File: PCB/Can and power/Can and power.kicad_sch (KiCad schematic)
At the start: 31 parts, among them J1 TPS54232DR, J2 ESP32, J3 12V, J4 C_H, J5 C_L, J6 GND, U1 SN65HVD230

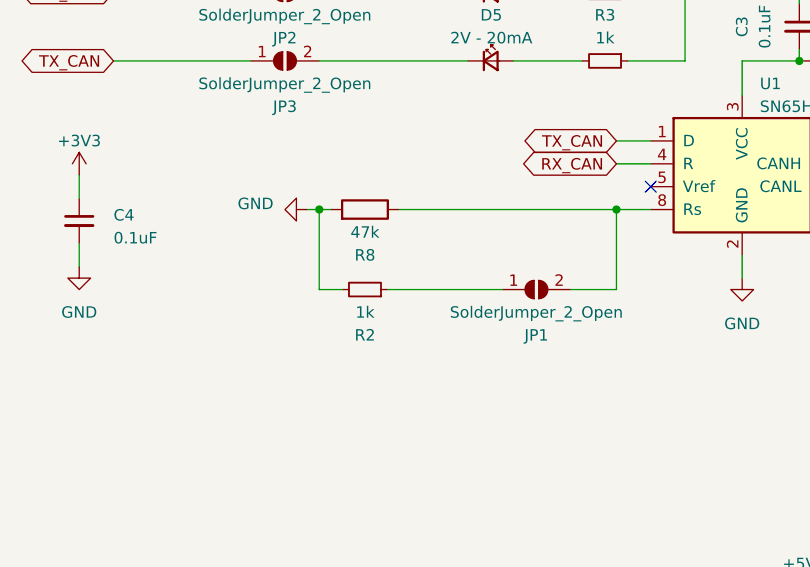
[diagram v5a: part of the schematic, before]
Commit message: Resistor correction
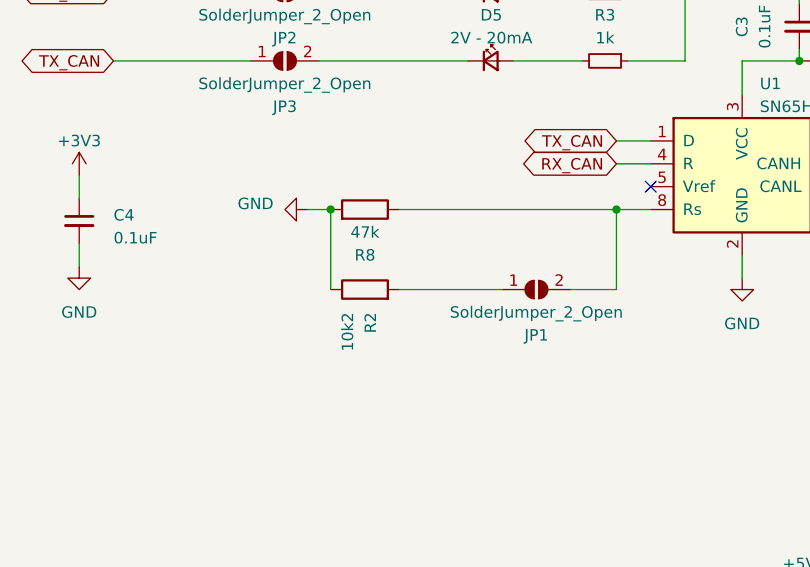
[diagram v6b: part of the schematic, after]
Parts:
- removed R2: 1k, Resistor_SMD:R_0603_1608Metric, symbol Device:R_Small
- added R2: 10k2, Resistor_SMD:R_0603_1608Metric, symbol Device:R
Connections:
- net GND: now also R2.1
- net at JP1.1 (A): now also R2.2
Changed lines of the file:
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@@
   (junction (at 153.67 143.51) (diameter 0) (color 0 0 0 0)
   )
-  (junction (at 144.78 72.39) (diameter 0) (color 0 0 0 0)
+  (junction (at 146.05 72.39) (diameter 0) (color 0 0 0 0)
   )
   (junction (at 198.12 119.38) (diameter 0) (color 0 0 0 0)
@@
     (stroke (width 0) (type default))
   )
+  (wire (pts (xy 153.67 81.28) (xy 165.1 81.28))
+    (stroke (width 0) (type default))
+  )
   (wire (pts (xy 60.96 163.83) (xy 66.04 163.83))
     (stroke (width 0) (type default))
@@
     (stroke (width 0) (type default))
   )
-  (wire (pts (xy 152.4 81.28) (xy 165.1 81.28))
-    (stroke (width 0) (type default))
-  )
   (wire (pts (xy 179.07 55.88) (xy 185.42 55.88))
     (stroke (width 0) (type default))
@@
     (stroke (width 0) (type default))
   )
-  (wire (pts (xy 144.78 72.39) (xy 143.51 72.39))
-    (stroke (width 0) (type default))
-  )
   (wire (pts (xy 121.92 48.26) (xy 137.16 48.26))
     (stroke (width 0) (type default))
   )
-  (wire (pts (xy 144.78 81.28) (xy 144.78 72.39))
-    (stroke (width 0) (type default))
-  )
   (wire (pts (xy 31.75 161.29) (xy 40.64 161.29))
     (stroke (width 0) (type default))
@@
     (stroke (width 0) (type default))
   )
+  (wire (pts (xy 143.51 72.39) (xy 146.05 72.39))
+    (stroke (width 0) (type default))
+  )
   (wire (pts (xy 207.01 119.38) (xy 207.01 120.65))
     (stroke (width 0) (type default))
@@
     (stroke (width 0) (type default))
   )
-  (wire (pts (xy 147.32 81.28) (xy 144.78 81.28))
-    (stroke (width 0) (type default))
-  )
   (wire (pts (xy 172.72 81.28) (xy 177.8 81.28))
     (stroke (width 0) (type default))
@@
     (stroke (width 0) (type default))
   )
-  (wire (pts (xy 146.05 72.39) (xy 144.78 72.39))
+  (wire (pts (xy 146.05 72.39) (xy 146.05 81.28))
     (stroke (width 0) (type default))
   )
@@
     )
   )
+  (symbol (lib_id "Device:R") (at 149.86 81.28 90) (unit 1)
+    (in_bom yes) (on_board yes) (dnp no)
+    (property "Reference" "R2" (at 150.495 83.82 0)
+      (effects (font (size 1.27 1.27)) (justify right))
+    )
+    (property "Value" "10k2" (at 147.955 83.82 0)
+      (effects (font (size 1.27 1.27)) (justify right))
+    )
+    (property "Footprint" "Resistor_SMD:R_0603_1608Metric" (at 149.86 83.058 90)
+      (effects (font (size 1.27 1.27)) hide)
+    )
+    (property "Datasheet" "https://www.yageo.com/upload/media/product/products/datasheet/rchip/PYu-RC_Group_51_RoHS_L_12.pdf" (at 149.86 81.28 0)
+      (effects (font (size 1.27 1.27)) hide)
+    )
+    (property "Description" "RES 10.2K OHM 1% 1/10W 0603" (at 149.86 81.28 0)
+      (effects (font (size 1.27 1.27)) hide)
+    )
+    (property "Manufacturer_Name" "YAGEO" (at 149.86 81.28 0)
+      (effects (font (size 1.27 1.27)) hide)
+    )
+    (property "Manufacturer_Part_Number" "RC0603FR-0710K2L" (at 149.86 81.28 0)
+      (effects (font (size 1.27 1.27)) hide)
+    )
+    (pin "1")
+    (pin "2")
+    (instances
+      (project "Can and power"
+        (path "/81a7cfcd-072f-485b-9296-819a4dd752de"
+          (reference "R2") (unit 1)
+        )
+      )
+    )
+  )
   (symbol (lib_id "Device:R") (at 149.86 72.39 270) (mirror x) (unit 1)
     (in_bom yes) (on_board yes) (dnp no)
@@
         )
       )
-    )
-  )
-  (symbol (lib_id "Device:R_Small") (at 149.86 81.28 270) (mirror x) (unit 1)
-    (in_bom yes) (on_board yes) (dnp no)
-    (property "Reference" "R2" (at 149.86 86.36 90)
-      (effects (font (size 1.27 1.27)))
-    )
-    (property "Value" "1k" (at 149.86 83.82 90)
-      (effects (font (size 1.27 1.27)))
-    )
-    (property "Footprint" "Resistor_SMD:R_0603_1608Metric" (at 149.86 81.28 0)
-      (effects (font (size 1.27 1.27)) hide)
-    )
-    (property "Datasheet" "https://www.yageo.com/upload/media/product/products/datasheet/rchip/PYu-RC_Group_51_RoHS_L_12.pdf" (at 149.86 81.28 0)
-      (effects (font (size 1.27 1.27)) hide)
-    )
-    (property "Description" "RES 1K OHM 1% 1/10W 0603" (at 149.86 81.28 0)
-      (effects (font (size 1.27 1.27)) hide)
-    )
-    (property "Manufacturer_Name" "YAGEO" (at 149.86 81.28 0)
-      (effects (font (size 1.27 1.27)) hide)
-    )
-    (property "Manufacturer_Part_Number" "RC0603FR-071KL" (at 149.86 81.28 0)
-      (effects (font (size 1.27 1.27)) hide)
-    )
-    (pin "1")
-    (pin "2")
-    (instances
-      (project "Can and power"
-        (path "/81a7cfcd-072f-485b-9296-819a4dd752de"
-          (reference "R2") (unit 1)
-        )
-      )

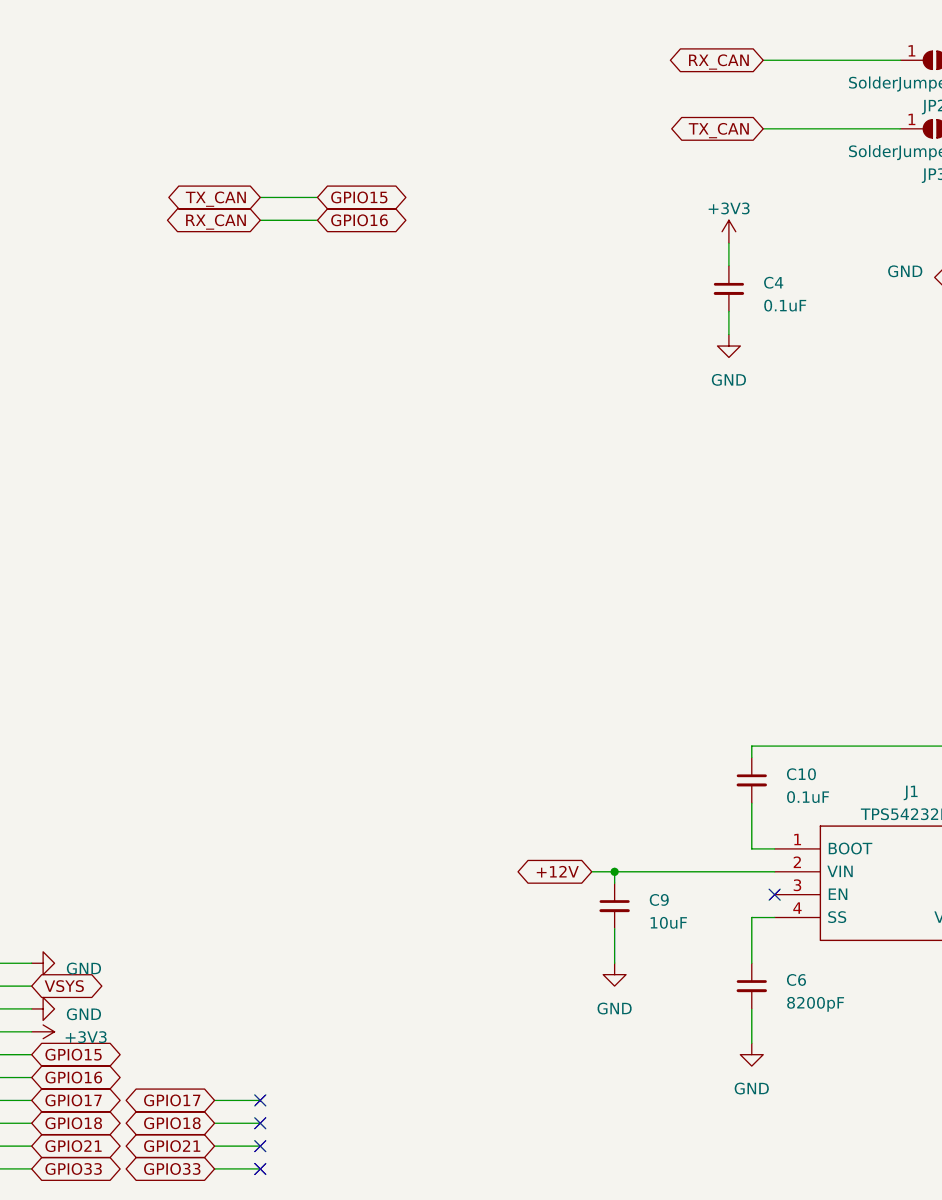
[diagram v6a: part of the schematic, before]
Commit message: New shield design
New shield design. MCP2515 is gone and transceiver has moved to SN65HVD230
Enable pin on the converter is used to cut off the uC when below 12V. Resistor values may have to change.
No real protection on start up stage -> might need another layer for that
Updated INO to reflect the changes in pinout
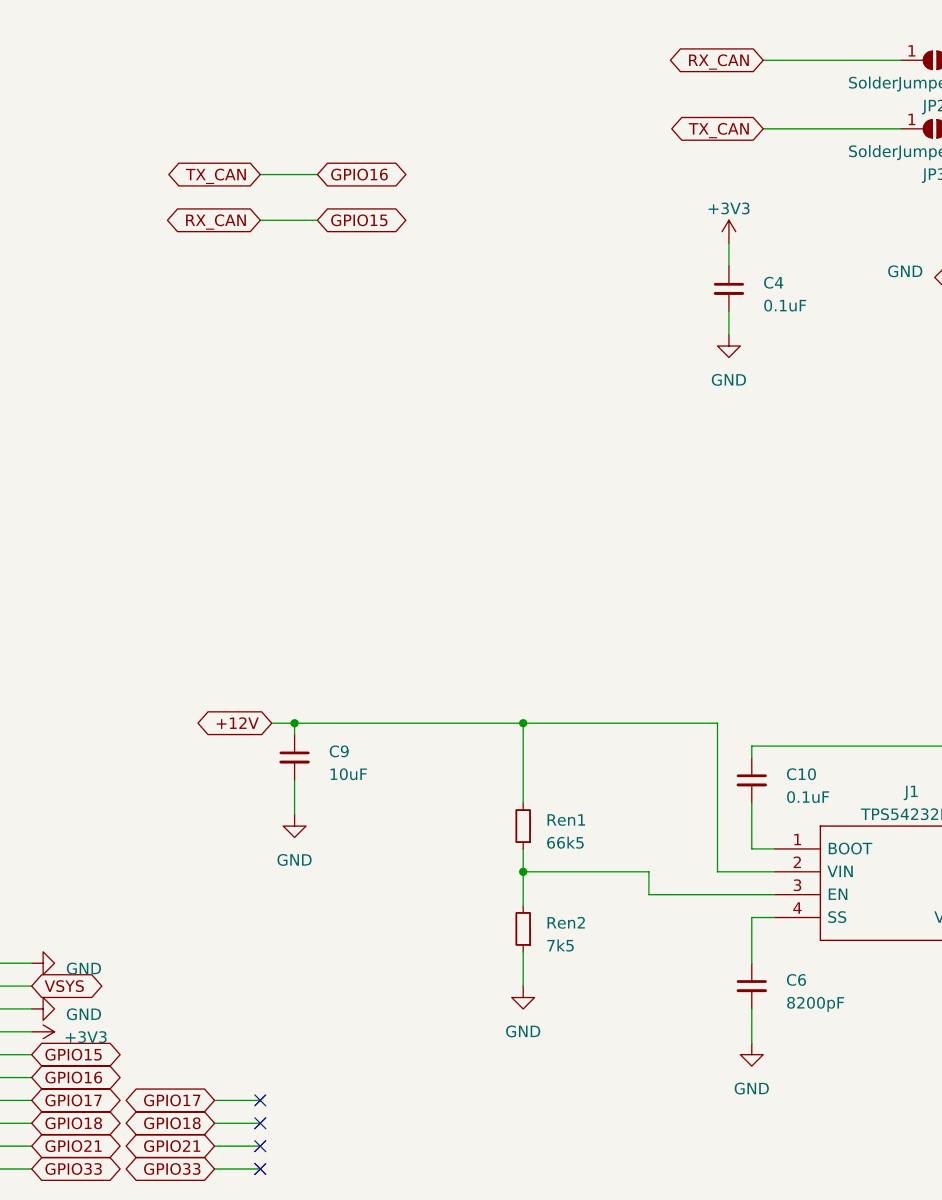
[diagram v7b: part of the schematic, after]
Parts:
- added Ren1: 66k5, Resistor_SMD:R_0603_1608Metric, symbol Device:R_Small
- added Ren2: 7k5, Resistor_SMD:R_0603_1608Metric, symbol Device:R_Small
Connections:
- net +12V: now also Ren1.2
- net GND: now also Ren2.1
- net GPIO15: now also JP2.1 (A), U1.4 (R); no longer JP3.1 (A), U1.1 (D)
- net GPIO16: now also JP3.1 (A), U1.1 (D); no longer JP2.1 (A), U1.4 (R)
- net at J1.3 (EN): now also Ren1.1, Ren2.2
- no-connect marks 6 -> 5
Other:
- moved on the sheet: C9

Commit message: CAD reference update
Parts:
- U1: Manufacturer_Name (none) -> Texas Instruments; Manufacturer_Part_Number (none) -> SN65HVD230
